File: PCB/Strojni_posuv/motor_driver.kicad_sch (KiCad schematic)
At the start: 5 parts, among them IC1 TB6600HG, U5 ISOM8711, U6 PC817, U7 74HC14

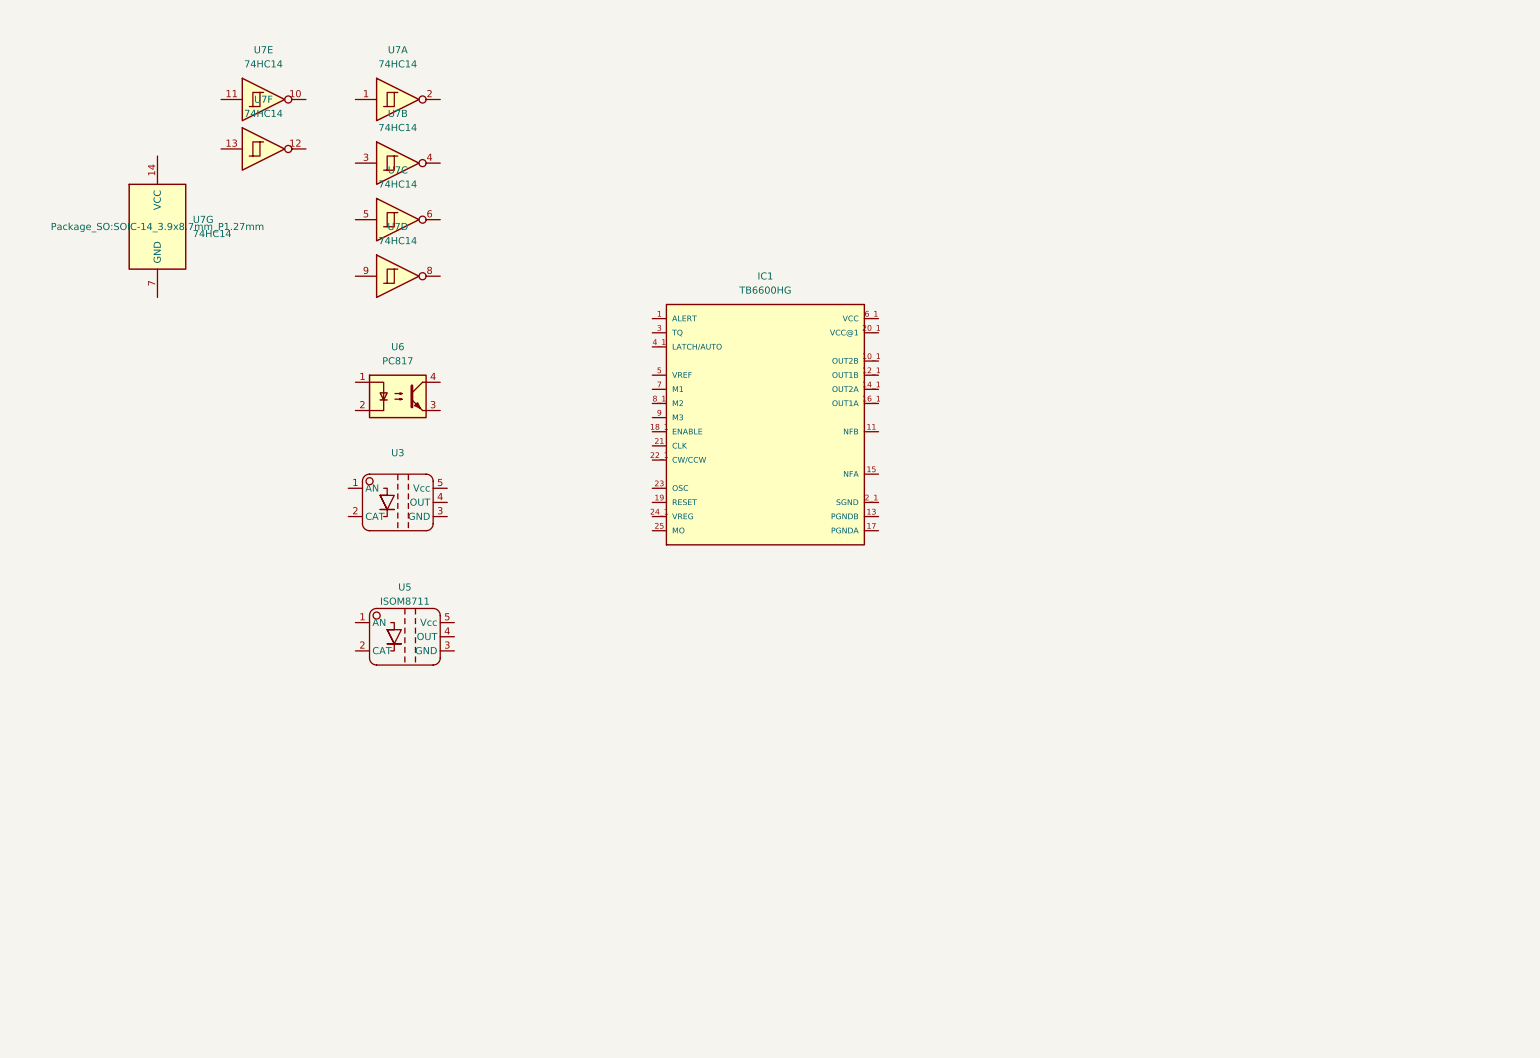
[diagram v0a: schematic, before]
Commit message: PCB making #3 Whole motor driver, small power changes, STM32 clock and new pin configuration
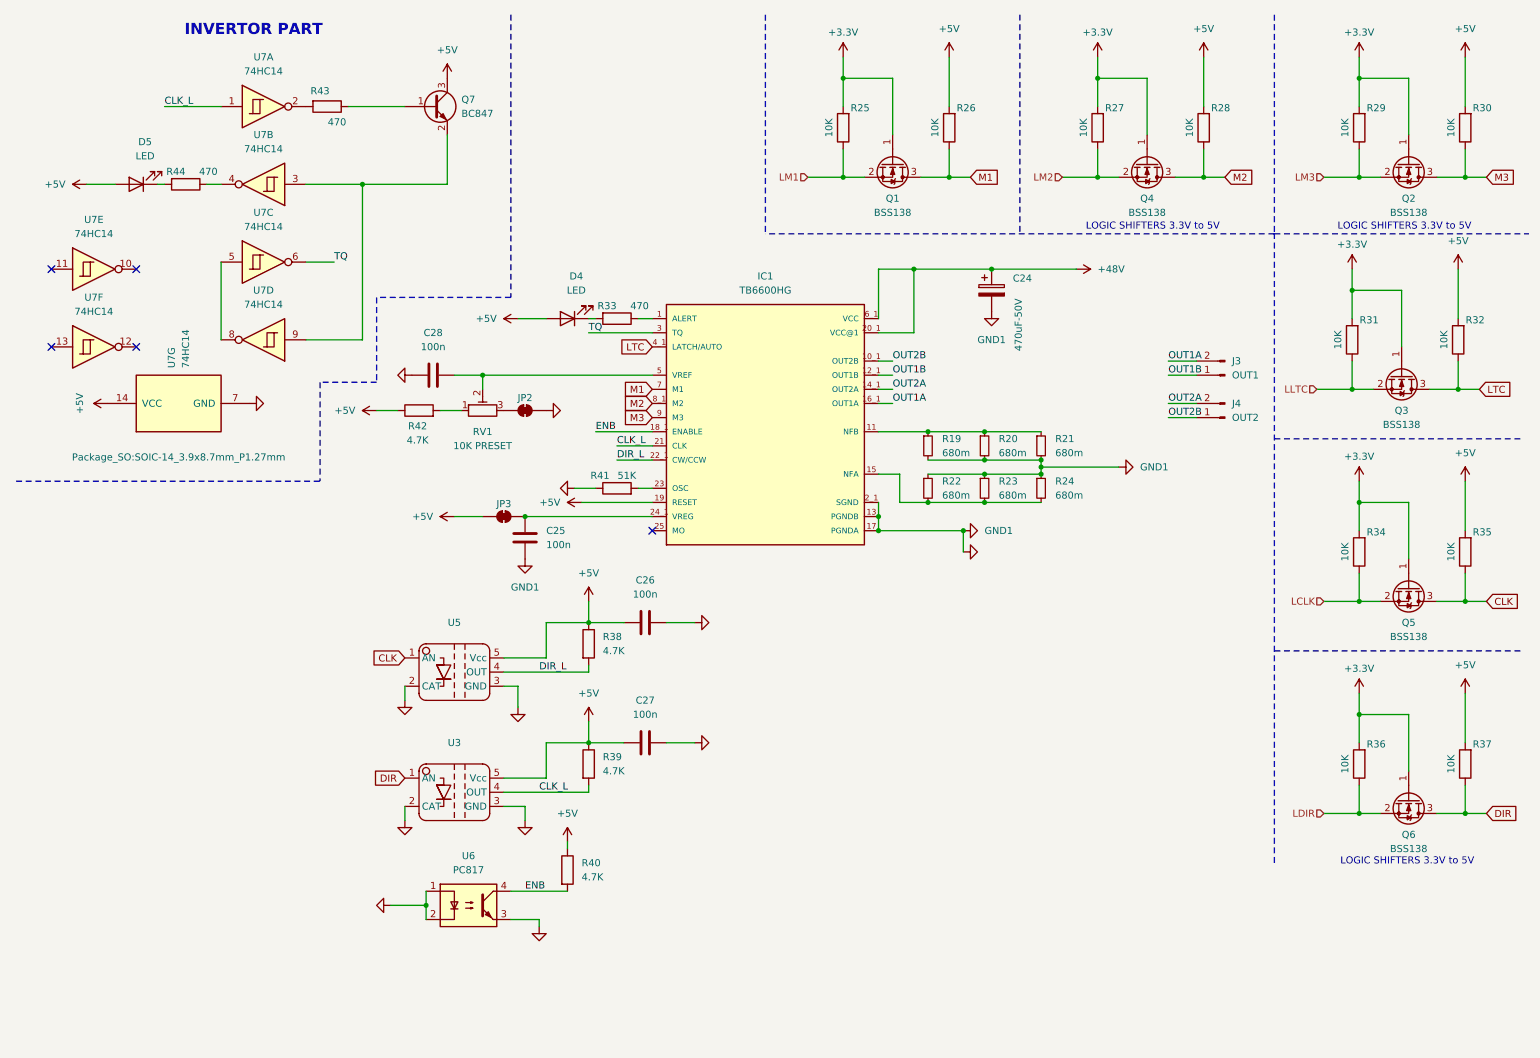
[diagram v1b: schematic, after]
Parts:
- added C24: 470uF-50V, symbol Device:C_Polarized
- added C25, C26, C27, C28: 100n, symbol Device:C
- added D4, D5: LED, symbol Device:LED
- added J3: OUT1, symbol Connector:Conn_01x02_Pin
- added J4: OUT2, symbol Connector:Conn_01x02_Pin
- added JP2, JP3: SolderJumper_2_Bridged, symbol Jumper:SolderJumper_2_Bridged
- added Q1, Q2, Q3, Q4, Q5, Q6: BSS138, Package_TO_SOT_SMD:SOT-23, symbol Transistor_FET:BSS138
- added Q7: BC847, Package_TO_SOT_SMD:SOT-23, symbol Transistor_BJT:BC847
- added R19, R20, R21, R22, R23, R24: 680m, symbol Device:R_Small
- added R25, R26, R27, R28, R29, R30, R31, R32, R34, R35, R36, R37: 10K, symbol Device:R
- added R33, R43, R44: 470, symbol Device:R
- added R38, R39, R40, R42: 4.7K, symbol Device:R
- added R41: 51K, symbol Device:R
- added RV1: 10K PRESET, symbol Device:R_Potentiometer_Trim
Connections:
- net at IC1.1 (ALERT): now also R33.1
- net OUT2B: now reaches IC1.10_1 (OUT2B)
- net OUT2B: now also J4.1 (Pin_1)
- net at IC1.11 (NFB): now also R19.1, R20.1, R21.1
- net OUT1B: now reaches IC1.12_1 (OUT1B)
- net OUT1B: now also J3.1 (Pin_1)
- net GND: now reaches IC1.13 (PGNDB)
- net GND: now also IC1.17 (PGNDA), IC1.2_1 (SGND), U3.2 (CAT), U3.3 (GND), U5.2 (CAT), U5.3 (GND), U6.1, U6.2, U6.3, U7.7 (GND), C24.2, C25.1, C26.1, C27.1, C28.2, JP2.2 (B), R19.2, R20.2, R21.2, R22.1, R23.1, R24.1, R41.1
- net OUT2A: now reaches IC1.14_1 (OUT2A)
- net OUT2A: now also J4.2 (Pin_2)
- net at IC1.15 (NFA): now also R22.2, R23.2, R24.2
- net OUT1A: now reaches IC1.16_1 (OUT1A)
- net OUT1A: now also J3.2 (Pin_2)
- net ENB: now reaches IC1.18_1 (ENABLE)
- net ENB: now also U6.4, R40.2
- net +5V: now reaches IC1.19 (RESET)
- net +5V: now also U3.5 (Vcc), U5.5 (Vcc), U7.14 (VCC), C26.2, C27.2, D4.2 (A), D5.2 (A), JP3.1 (A), Q7.3 (C), R26.2, R28.2, R30.2, R32.2, R35.2, R37.2, R38.1, R39.1, R40.1, R42.1
- net +48V: now reaches IC1.20_1 (VCC@1)
- net +48V: now also IC1.6_1 (VCC), C24.1
- net CLK_L: now reaches IC1.21 (CLK)
- net CLK_L: now also U3.4 (OUT), U7.1, R39.2
- net DIR_L: now reaches IC1.22_1 (CW/CCW)
- net DIR_L: now also U5.4 (OUT), R38.2
- net at IC1.23 (OSC): now also R41.2
- net at IC1.24_1 (VREG): now also C25.2, JP3.2 (B)
- net TQ: now reaches IC1.3 (TQ)
- net TQ: now also U7.6
- net LTC: now reaches IC1.4_1 (LATCH/AUTO)
- net LTC: now also Q3.3 (D), R32.1
- net at IC1.5 (VREF): now also C28.1, RV1.2
- net M1: now reaches IC1.7 (M1)
- net M1: now also Q1.3 (D), R26.1
- net M2: now reaches IC1.8_1 (M2)
- net M2: now also Q4.3 (D), R28.1
- net M3: now reaches IC1.9 (M3)
- net M3: now also Q2.3 (D), R30.1
- net at U7.8: now also U7.5
- net at U7.9: now also U7.3, Q7.2 (E)
- net at U7.2: now also R43.2
- net at U7.4: now also R44.1
- net DIR: now reaches U3.1 (AN)
- net DIR: now also Q6.3 (D), R37.1
- net CLK: now reaches U5.1 (AN)
- net CLK: now also Q5.3 (D), R35.1
- new net: JP2.1 (A), RV1.3
- new net: Q7.1 (B), R43.1
- new net: D4.1 (K), R33.2
- new net: D5.1 (K), R44.2
- new net: R42.2, RV1.1
- new net +3.3V: Q1.1 (G), Q2.1 (G), Q3.1 (G), Q4.1 (G), Q5.1 (G), Q6.1 (G), R25.2, R27.2, R29.2, R31.2, R34.2, R36.2
- new net LCLK: Q5.2 (S), R34.1
- new net LDIR: Q6.2 (S), R36.1
- new net LLTC: Q3.2 (S), R31.1
- new net LM1: Q1.2 (S), R25.1
- new net LM2: Q4.2 (S), R27.1
- new net LM3: Q2.2 (S), R29.1
- no-connect marks 0 -> 5
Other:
- note added: "INVERTOR PART"
- note added: "LOGIC SHIFTERS 3.3V to 5V"
- moved on the sheet: U3, U5, U6, U7A, U7B, U7C, U7D, U7E, U7F, U7G

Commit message: PCB making #4 Finding components on JLCPCB and adding their tags to schematic. Assigning almost all footprints
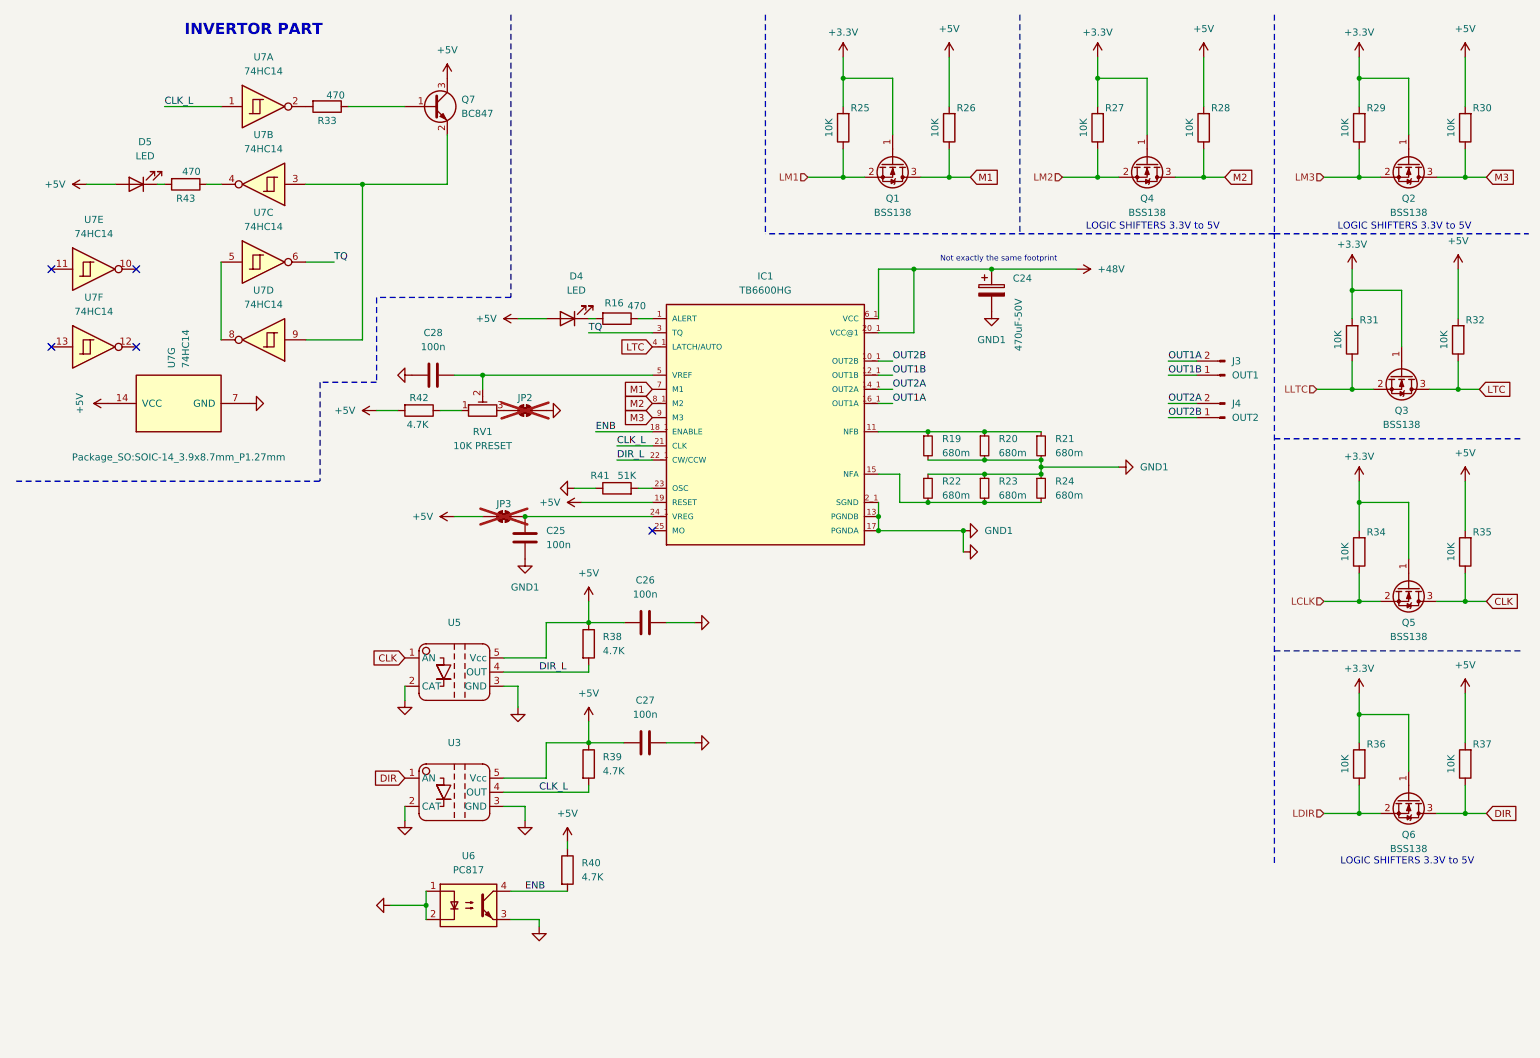
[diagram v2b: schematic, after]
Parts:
- removed R44: 470, symbol Device:R
- added R16: 470, Resistor_SMD:R_0603_1608Metric, symbol Device:R
- C24: footprint (none) -> StuffBench:CP_Elec_12.5x16; LCSC (none) -> C249547
- C25, C26, C27, C28: footprint (none) -> Capacitor_SMD:C_0603_1608Metric; LCSC (none) -> C14663
- D4, D5: footprint (none) -> LED_SMD:LED_0603_1608Metric
- IC1: Availability In Stock -> (none); Check_prices https://www.snapeda.com/parts/TB6600HG/Toshiba+Semiconducto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 -> (none); Description_1 Bipolar Motor Driver Power MOSFET Parallel 25-HZIP -> (none); LCSC (none) -> C66042; MF Toshiba -> (none); MP TB6600HG -> (none); Package SIP-25 Toshiba -> (none); Price None -> (none); Purchase-URL https://www.snapeda.com/api/url_track_click_mouser/?unipart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 -> (none); SnapEDA_Link https://www.snapeda.com/parts/TB6600HG/Toshiba+Semiconducto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 -> (none)
- JP2, JP3: footprint (none) -> Jumper:SolderJumper-2_P1.3mm_Bridged_RoundedPad1.0x1.5mm; now not fitted
- Q7: LCSC (none) -> C8664
- R19, R20, R21, R22, R23, R24: footprint (none) -> Resistor_SMD:R_1206_3216Metric; LCSC (none) -> C19108
- R25, R26, R27, R28, R29, R30, R31, R32, R34, R35, R36, R37: footprint (none) -> Resistor_SMD:R_0603_1608Metric; LCSC (none) -> C25804
- R33, R43: footprint (none) -> Resistor_SMD:R_0603_1608Metric; LCSC (none) -> C23179
- R38, R39, R40, R42: footprint (none) -> Resistor_SMD:R_0603_1608Metric; LCSC (none) -> C23162
- R41: footprint (none) -> Resistor_SMD:R_0603_1608Metric; LCSC (none) -> C23196
- U6: LCSC (none) -> C20612591
- U7: Field5 (none) -> C5605
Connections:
- net +5V: now also C26.1, C27.1, R42.2; no longer C26.2, C27.2, R42.1
- net GND: now also C25.2, C26.2, C27.2, C28.1; no longer C25.1, C26.1, C27.1, C28.2
- net at IC1.1 (ALERT): now also R16.1; no longer R33.1
- net at IC1.24_1 (VREG), JP3.2 (B): now also C25.1; no longer C25.2
- net at IC1.5 (VREF), RV1.2: now also C28.2; no longer C28.1
- net at Q7.1 (B): now also R33.1; no longer R43.1
- net at R43.2: now also D5.1 (K); no longer U7.2
- net at D4.1 (K): now also R16.2; no longer R33.2
- net at RV1.1: now also R42.1; no longer R42.2
- net at U7.4: now also R43.1
- new net: R33.2, U7.2
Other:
- note added: "Not exactly the same footprint"

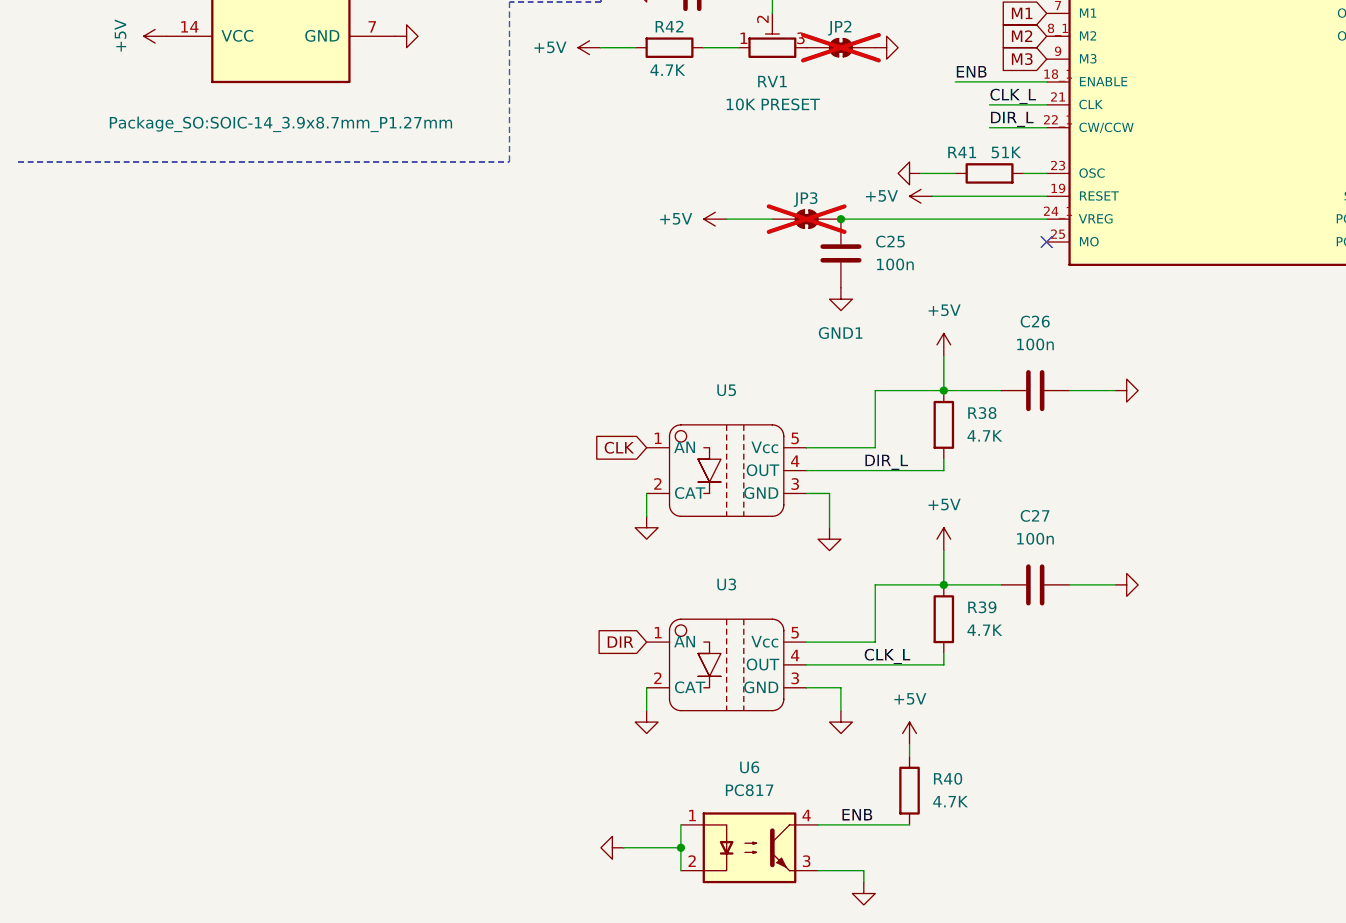
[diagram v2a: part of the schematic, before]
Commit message: PCB making #5 Starting with component placement
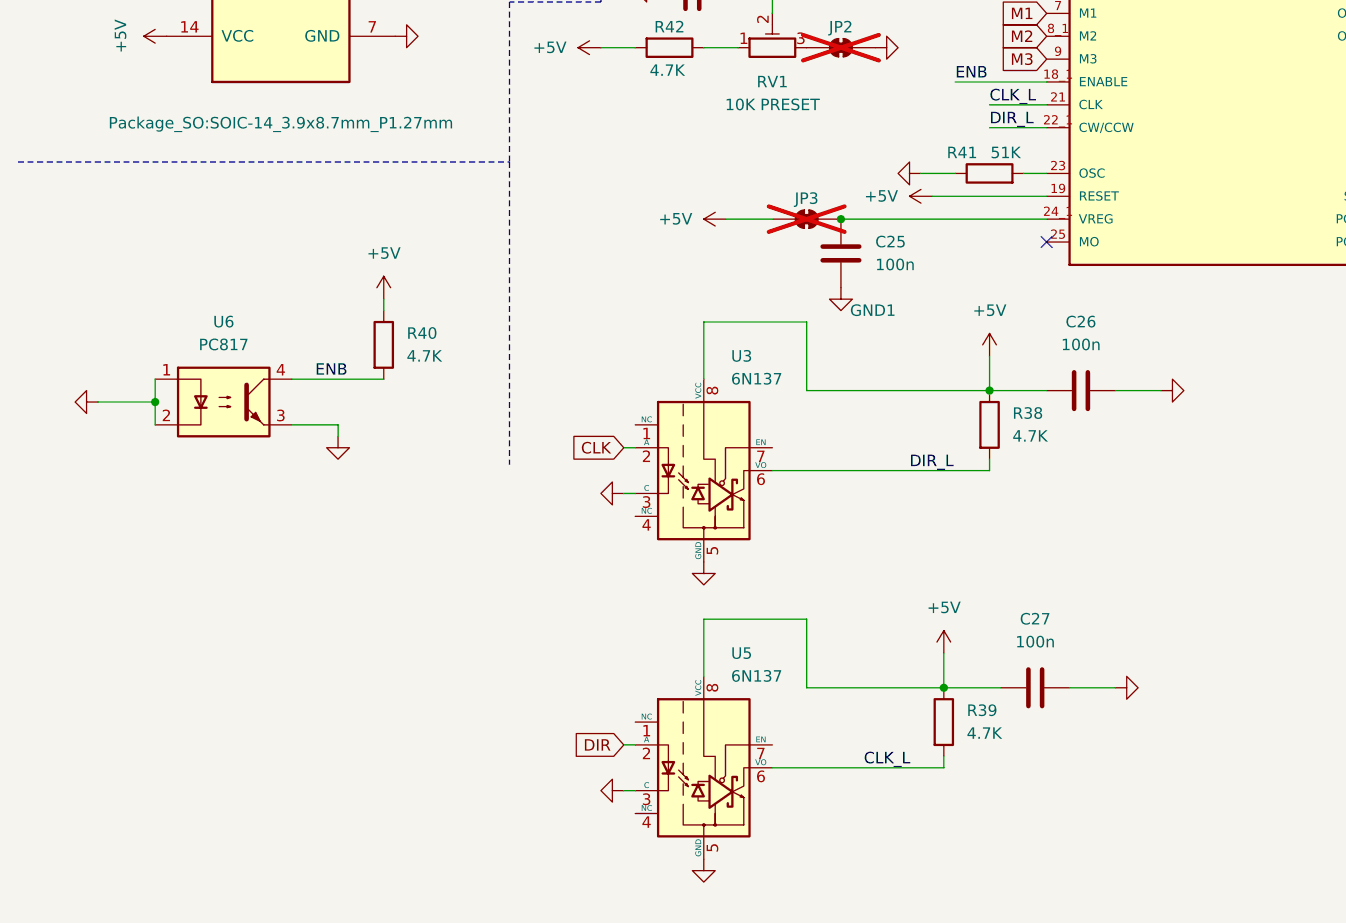
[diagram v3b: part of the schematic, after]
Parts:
- removed U3: ~, symbol Motor_stuffs:ISOM8711
- removed U5: ISOM8711, symbol Motor_stuffs:ISOM8711
- added U3, U5: 6N137, Package_SO:SOP-8_6.605x9.655mm_P2.54mm, symbol Isolator:6N137
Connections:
- net +5V: now also U3.8 (VCC), U5.8 (VCC)
- net CLK: now also U3.2 (A)
- net CLK_L: now also U5.6 (VO)
- net DIR: now also U5.2 (A)
- net DIR_L: now also U3.6 (VO)
- net GND: now also U3.3 (C), U3.5 (GND), U5.3 (C), U5.5 (GND)
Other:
- moved on the sheet: C26, C27, R38, R39, R40, U6
